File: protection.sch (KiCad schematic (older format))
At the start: 5 parts, among them Q1 DMP3098L

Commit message: Update the README, add a new rendered image of the board
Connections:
- net labels added: RP_G
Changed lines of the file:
@@
 Text Notes 2500 2700 0    50   ~ 0
 TVS should be sufficient\nto survive even some\nload dumps, at least in\nconjunction with the\npolyfuse.
-Text Notes 3750 850  0    50   ~ 0
+Text Notes 3650 950  0    50   ~ 0
 Reverse polarity protection
 Connection ~ 3350 1300
@@
 	0    1    -1   0
 $EndComp
+Text Label 4150 1650 2    50   ~ 0
+RP_G
 $EndSCHEMATC

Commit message: Make protection TVS bidirectional
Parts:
- removed D1: TPSMD16A, Diode_SMD:D_SMC, symbol Device:D_Zener
- added D1: 5.0SMDJ16CA, Diode_SMD:D_SMC, symbol Device:D_TVS
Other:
- note removed: "Fuse slightly overspecced \nregarding NMEA2000 1A\nmaximum due to strong\ntemperature derating of \npolyfuses."
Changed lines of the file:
@@
 	1    0    0    -1
-$EndComp
-$Comp
-L Device:D_Zener D?
-U 1 1 5E467AD0
-P 3000 1600
-AR Path="/5E467AD0" Ref="D?"  Part="1"
-AR Path="/5E460E30/5E467AD0" Ref="D1"  Part="1"
-F 0 "D1" V 2950 1800 50  0000 R CNN
-F 1 "TPSMD16A" V 3050 2100 50  0000 R CNN
-F 2 "Diode_SMD:D_SMC" H 3000 1600 50  0001 C CNN
-F 3 "~" H 3000 1600 50  0001 C CNN
-	1    3000 1600
-	0    -1   1    0
 $EndComp
 Wire Wire Line
@@
 Text HLabel 4900 1300 2    50   Output ~ 0
 12V_protected
-Text Notes 1500 1050 0    50   ~ 0
-Fuse slightly overspecced \nregarding NMEA2000 1A\nmaximum due to strong\ntemperature derating of \npolyfuses.
 Text Notes 2500 2700 0    50   ~ 0
 TVS should be sufficient\nto survive even some\nload dumps, at least in\nconjunction with the\npolyfuse.
@@
 Text Label 4150 1650 2    50   ~ 0
 RP_G
+$Comp
+L Device:D_TVS D1
+U 1 1 5E5A3FFE
+P 3000 1600
+F 0 "D1" V 2954 1679 50  0000 L CNN
+F 1 "5.0SMDJ16CA" V 3045 1679 50  0000 L CNN
+F 2 "Diode_SMD:D_SMC" H 3000 1600 50  0001 C CNN
+F 3 "~" H 3000 1600 50  0001 C CNN
+	1    3000 1600
+	0    1    1    0
+$EndComp
 $EndSCHEMATC

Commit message: Add LCSC part numbers to components
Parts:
- D1: LCSC (none) -> C284067
- D8: LCSC (none) -> C118608
- F1: LCSC (none) -> C135376
- Q1: LCSC (none) -> C130884
- R5: LCSC (none) -> C25803
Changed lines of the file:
@@
 F 2 "Fuse:Fuse_2920_7451Metric" V 1780 1300 50  0001 C CNN
 F 3 "~" H 1850 1300 50  0001 C CNN
+F 4 "C135376" H 1850 1300 50  0001 C CNN "LCSC"
 	1    1850 1300
 	0    1    1    0
@@
 F 2 "Package_TO_SOT_SMD:SOT-23" H 4350 1325 50  0001 L CIN
 F 3 "" H 4150 1400 50  0001 L CNN
+F 4 "C130884" H 4150 1400 50  0001 C CNN "LCSC"
 	1    4150 1400
 	0    -1   -1   0
@@
 F 2 "Diode_SMD:D_SOD-323" H 4400 1450 50  0001 C CNN
 F 3 "https://datasheet.lcsc.com/szlcsc/SK-MM3Z10_C216753.pdf" H 4400 1450 50  0001 C CNN
+F 4 "C118608" H 4400 1450 50  0001 C CNN "LCSC"
 	1    4400 1450
 	0    1    1    0
@@
 F 2 "Resistor_SMD:R_0603_1608Metric_Pad1.05x0.95mm_HandSolder" V 4080 1850 50  0001 C CNN
 F 3 "~" H 4150 1850 50  0001 C CNN
+F 4 "C25803" H 4150 1850 50  0001 C CNN "LCSC"
 	1    4150 1850
 	1    0    0    -1
@@
 F 2 "Diode_SMD:D_SMC" H 3000 1600 50  0001 C CNN
 F 3 "~" H 3000 1600 50  0001 C CNN
+F 4 "C284067" H 3000 1600 50  0001 C CNN "LCSC"
 	1    3000 1600
 	0    1    1    0

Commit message: Isolated CAN bus implementation
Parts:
- D1: value 5.0SMDJ16CA -> 5.0SMDJ20CA
- F1: value 2920L110/60MR (1.1A) -> ASMD2920-185; symbol Device:Fuse -> Device:Polyfuse; LCSC C135376 -> C135379
- R5: footprint Resistor_SMD:R_0603_1608Metric_Pad1.05x0.95mm_HandSolder -> Resistor_SMD:R_0603_1608Metric
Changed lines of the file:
@@
 $Descr A4 11693 8268
 encoding utf-8
-Sheet 7 7
+Sheet 6 7
 Title ""
 Date ""
@@
 $EndDescr
 $Comp
-L Device:Fuse F?
+L Device:Polyfuse F?
 U 1 1 5E467AC2
 P 1850 1300
@@
 AR Path="/5E460E30/5E467AC2" Ref="F1"  Part="1"
 F 0 "F1" V 1653 1300 50  0000 C CNN
-F 1 "2920L110/60MR (1.1A)" V 1744 1300 50  0000 C CNN
+F 1 "ASMD2920-185" V 1744 1300 50  0000 C CNN
 F 2 "Fuse:Fuse_2920_7451Metric" V 1780 1300 50  0001 C CNN
 F 3 "~" H 1850 1300 50  0001 C CNN
-F 4 "C135376" H 1850 1300 50  0001 C CNN "LCSC"
+F 4 "C135379" H 1850 1300 50  0001 C CNN "LCSC"
 	1    1850 1300
 	0    1    1    0
@@
 F 0 "R5" H 4220 1896 50  0000 L CNN
 F 1 "100k" H 4220 1805 50  0000 L CNN
-F 2 "Resistor_SMD:R_0603_1608Metric_Pad1.05x0.95mm_HandSolder" V 4080 1850 50  0001 C CNN
+F 2 "Resistor_SMD:R_0603_1608Metric" V 4080 1850 50  0001 C CNN
 F 3 "~" H 4150 1850 50  0001 C CNN
 F 4 "C25803" H 4150 1850 50  0001 C CNN "LCSC"
@@
 P 3000 1600
 F 0 "D1" V 2954 1679 50  0000 L CNN
-F 1 "5.0SMDJ16CA" V 3045 1679 50  0000 L CNN
+F 1 "5.0SMDJ20CA" V 3045 1679 50  0000 L CNN
 F 2 "Diode_SMD:D_SMC" H 3000 1600 50  0001 C CNN
 F 3 "~" H 3000 1600 50  0001 C CNN

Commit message: Parts updated to match JLCPCB availability
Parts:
- D8: LCSC C118608 -> C235983
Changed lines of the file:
@@
 F 2 "Diode_SMD:D_SOD-323" H 4400 1450 50  0001 C CNN
 F 3 "https://datasheet.lcsc.com/szlcsc/SK-MM3Z10_C216753.pdf" H 4400 1450 50  0001 C CNN
-F 4 "C118608" H 4400 1450 50  0001 C CNN "LCSC"
+F 4 "C235983" H 4400 1450 50  0001 C CNN "LCSC"
 	1    4400 1450
 	0    1    1    0

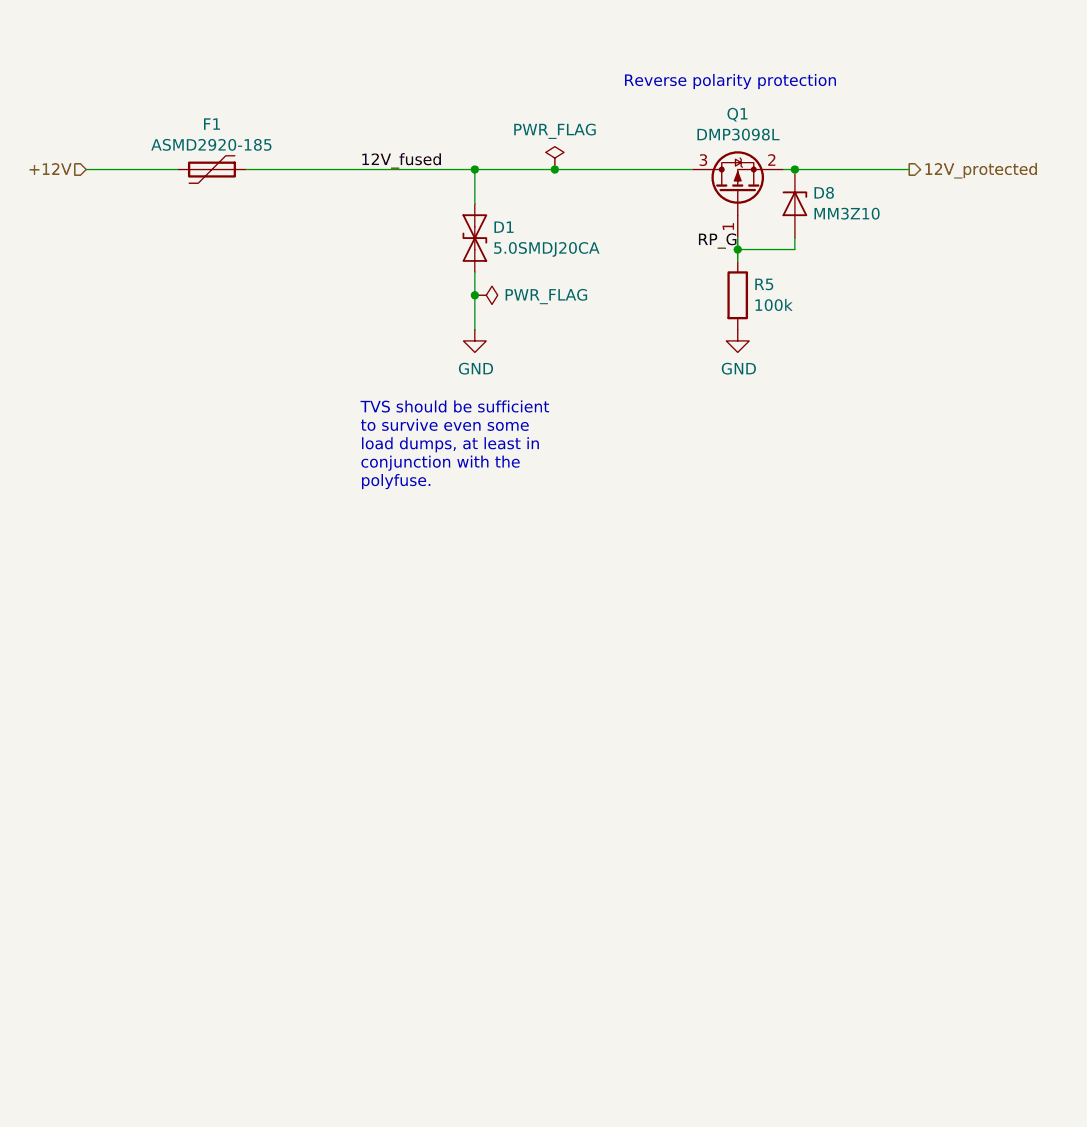
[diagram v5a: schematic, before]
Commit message: Revert back to using INA199 as a current limiter
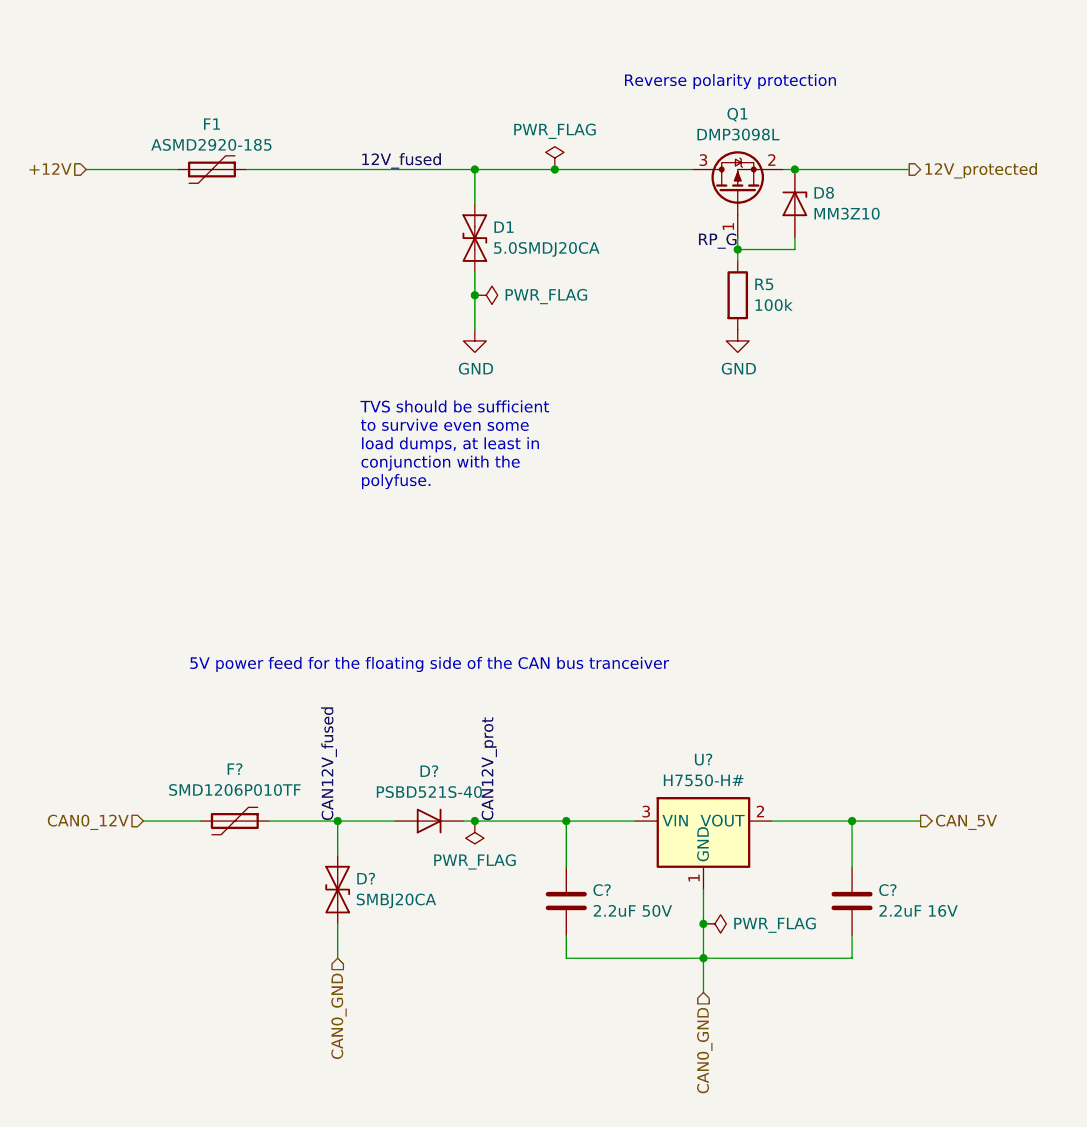
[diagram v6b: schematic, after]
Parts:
- added C?: 2.2uF 50V, Capacitor_SMD:C_1206_3216Metric, symbol Device:C
- added C?: 2.2uF 16V, Capacitor_SMD:C_0603_1608Metric, symbol Device:C
- added D?: SMBJ20CA, Diode_SMD:D_SMB, symbol Device:D_TVS
- added D?: PSBD521S-40, Diode_SMD:D_SOD-523, symbol Device:D
- added F?: SMD1206P010TF, Fuse:Fuse_1206_3216Metric, symbol Device:Polyfuse
- added U?: H7550-H#, Package_TO_SOT_SMD:SOT-23, symbol sailor-hat:HT75xx-1-SOT23
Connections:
- new net CAN0_12V: F?.2
- new net CAN0_GND: C?.2, C?.2, D?.2 (A2), U?.1 (GND)
- new net CAN12V_fused: D?.1 (A1), D?.2 (A), F?.1
- new net CAN12V_prot: C?.1, D?.1 (K), U?.3 (VIN)
- new net CAN_5V: C?.1, U?.2 (VOUT)
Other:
- note added: "5V power feed for the floating side of the CAN bus tranceiver"
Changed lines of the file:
@@
 	0    1    1    0
 $EndComp
+$Comp
+L sailor-hat:HT75xx-1-SOT23 U?
+U 1 1 5F59D8E6
+P 4000 4250
+AR Path="/5C348474/5F59D8E6" Ref="U?"  Part="1"
+AR Path="/5E460E30/5F59D8E6" Ref="U?"  Part="1"
+F 0 "U?" H 4000 4617 50  0000 C CNN
+F 1 "H7550-H#" H 4000 4526 50  0000 C CNN
+F 2 "Package_TO_SOT_SMD:SOT-23" H 4000 4575 50  0001 C CIN
+F 3 "" H 4000 4350 50  0001 C CNN
+F 4 "C277875" H 4000 4250 50  0001 C CNN "LCSC"
+	1    4000 4250
+	1    0    0    -1
+$EndComp
+$Comp
+L Device:Polyfuse F?
+U 1 1 5F59D8ED
+P 1950 4150
+AR Path="/5C348474/5F59D8ED" Ref="F?"  Part="1"
+AR Path="/5E460E30/5F59D8ED" Ref="F?"  Part="1"
+F 0 "F?" V 1725 4150 50  0000 C CNN
+F 1 "SMD1206P010TF" V 1816 4150 50  0000 C CNN
+F 2 "Fuse:Fuse_1206_3216Metric" H 2000 3950 50  0001 L CNN
+F 3 "~" H 1950 4150 50  0001 C CNN
+F 4 "C20981" H 1950 4150 50  0001 C CNN "LCSC"
+	1    1950 4150
+	0    1    1    0
+$EndComp
+$Comp
+L Device:D_TVS D?
+U 1 1 5F59D8F4
+P 2400 4450
+AR Path="/5C348474/5F59D8F4" Ref="D?"  Part="1"
+AR Path="/5E460E30/5F59D8F4" Ref="D?"  Part="1"
+F 0 "D?" V 2354 4529 50  0000 L CNN
+F 1 "SMBJ20CA" V 2445 4529 50  0000 L CNN
+F 2 "Diode_SMD:D_SMB" H 2400 4450 50  0001 C CNN
+F 3 "~" H 2400 4450 50  0001 C CNN
+F 4 "C113992" H 2400 4450 50  0001 C CNN "LCSC"
+	1    2400 4450
+	0    1    1    0
+$EndComp
+$Comp
+L Device:D D?
+U 1 1 5F59D8FB
+P 2800 4150
+AR Path="/5C348474/5F59D8FB" Ref="D?"  Part="1"
+AR Path="/5E460E30/5F59D8FB" Ref="D?"  Part="1"
+F 0 "D?" H 2800 3934 50  0000 C CNN
+F 1 "PSBD521S-40" H 2800 4025 50  0000 C CNN
+F 2 "Diode_SMD:D_SOD-523" H 2800 4150 50  0001 C CNN
+F 3 "~" H 2800 4150 50  0001 C CNN
+F 4 "C168633" H 2800 4150 50  0001 C CNN "LCSC"
+	1    2800 4150
+	-1   0    0    1
+$EndComp
+Wire Wire Line
+	2100 4150 2400 4150
+Wire Wire Line
+	2950 4150 3000 4150
+Wire Wire Line
+	4000 4900 4000 4750
+Wire Wire Line
+	2400 4300 2400 4150
+Connection ~ 2400 4150
+Wire Wire Line
+	2400 4150 2650 4150
+Wire Wire Line
+	2400 4600 2400 4750
+Text HLabel 1550 4150 0    50   Input ~ 0
+CAN0_12V
+Text HLabel 2400 4750 3    50   Input ~ 0
+CAN0_GND
+Text HLabel 4000 4900 3    50   Input ~ 0
+CAN0_GND
+Text Notes 1750 3500 0    50   ~ 0
+5V power feed for the floating side of the CAN bus tranceiver
+$Comp
+L power:PWR_FLAG #FLG?
+U 1 1 5F59D90D
+P 3000 4150
+AR Path="/5C348474/5F59D90D" Ref="#FLG?"  Part="1"
+AR Path="/5E460E30/5F59D90D" Ref="#FLG0107"  Part="1"
+F 0 "#FLG0107" H 3000 4225 50  0001 C CNN
+F 1 "PWR_FLAG" H 3000 4323 50  0000 C CNN
+F 2 "" H 3000 4150 50  0001 C CNN
+F 3 "~" H 3000 4150 50  0001 C CNN
+	1    3000 4150
+	-1   0    0    1
+$EndComp
+Connection ~ 3000 4150
+Wire Wire Line
+	3000 4150 3400 4150
+$Comp
+L power:PWR_FLAG #FLG?
+U 1 1 5F59D915
+P 4000 4600
+AR Path="/5C348474/5F59D915" Ref="#FLG?"  Part="1"
+AR Path="/5E460E30/5F59D915" Ref="#FLG0108"  Part="1"
+F 0 "#FLG0108" H 4000 4675 50  0001 C CNN
+F 1 "PWR_FLAG" V 4000 4728 50  0000 L CNN
+F 2 "" H 4000 4600 50  0001 C CNN
+F 3 "~" H 4000 4600 50  0001 C CNN
+	1    4000 4600
+	0    1    1    0
+$EndComp
+Connection ~ 4000 4600
+Wire Wire Line
+	4000 4600 4000 4450
+Wire Wire Line
+	1550 4150 1800 4150
+Text Label 2400 4150 1    50   ~ 0
+CAN12V_fused
+Text Label 3100 4150 1    50   ~ 0
+CAN12V_prot
+$Comp
+L Device:C C?
+U 1 1 5F59D921
+P 3400 4500
+AR Path="/5CA65CC5/5F59D921" Ref="C?"  Part="1"
+AR Path="/5C348474/5F59D921" Ref="C?"  Part="1"
+AR Path="/5E460E30/5F59D921" Ref="C?"  Part="1"
+F 0 "C?" H 3515 4546 50  0000 L CNN
+F 1 "2.2uF 50V" H 3515 4455 50  0000 L CNN
+F 2 "Capacitor_SMD:C_1206_3216Metric" H 3438 4350 50  0001 C CNN
+F 3 "~" H 3400 4500 50  0001 C CNN
+F 4 "C50254" H 3400 4500 50  0001 C CNN "LCSC"
+	1    3400 4500
+	1    0    0    -1
+$EndComp
+$Comp
+L Device:C C?
+U 1 1 5F59D928
+P 4650 4500
+AR Path="/5CA65CC5/5F59D928" Ref="C?"  Part="1"
+AR Path="/5C348474/5F59D928" Ref="C?"  Part="1"
+AR Path="/5E460E30/5F59D928" Ref="C?"  Part="1"
+F 0 "C?" H 4765 4546 50  0000 L CNN
+F 1 "2.2uF 16V" H 4765 4455 50  0000 L CNN
+F 2 "Capacitor_SMD:C_0603_1608Metric" H 4688 4350 50  0001 C CNN
+F 3 "~" H 4650 4500 50  0001 C CNN
+F 4 "C23630" H 4650 4500 50  0001 C CNN "LCSC"
+	1    4650 4500
+	1    0    0    -1
+$EndComp
+Wire Wire Line
+	3400 4350 3400 4150
+Connection ~ 3400 4150
+Wire Wire Line
+	3400 4150 3700 4150
+Wire Wire Line
+	4650 4350 4650 4150
+Wire Wire Line
+	4650 4150 4300 4150
+Wire Wire Line
+	4950 4150 4650 4150
+Connection ~ 4650 4150
+Wire Wire Line
+	3400 4650 3400 4750
+Wire Wire Line
+	3400 4750 4000 4750
+Connection ~ 4000 4750
+Wire Wire Line
+	4000 4750 4000 4600
+Wire Wire Line
+	4000 4750 4650 4750
+Wire Wire Line
+	4650 4750 4650 4650
+Text HLabel 4950 4150 2    50   Output ~ 0
+CAN_5V
 $EndSCHEMATC

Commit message: Make voltage protection circuitry 24V compliant
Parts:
- D1: value 5.0SMDJ20CA -> 5.0SMDJ36CA; LCSC C284067 -> C284112
- D10: renamed from D?; value SMBJ20CA -> SMBJ36CA; LCSC C113992 -> C114002
- D13: renamed from D?; value PSBD521S-40 -> SS210; footprint Diode_SMD:D_SOD-523 -> Diode_SMD:D_SMA; symbol Device:D -> Device:D_Schottky
- D8: value MM3Z10 -> MM3Z8V2; LCSC C235983 -> C118606
- Q1: value DMP3098L -> WST03P06; LCSC C130884 -> C105166
- gave numbers to parts that had none: 4
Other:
- note added: "5V power feed for the bus side of the CAN bus tranceiver"
- note removed: "5V power feed for the floating side of the CAN bus tranceiver"
- note removed: "TVS should be sufficient\nto survive even some\nload dumps, at least in\nconjunction with the\npolyfuse."
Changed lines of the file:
@@
 AR Path="/5E460E30/5E467ADC" Ref="Q1"  Part="1"
 F 0 "Q1" V 4492 1400 50  0000 C CNN
-F 1 "DMP3098L" V 4401 1400 50  0000 C CNN
+F 1 "WST03P06" V 4401 1400 50  0000 C CNN
 F 2 "Package_TO_SOT_SMD:SOT-23" H 4350 1325 50  0001 L CIN
 F 3 "" H 4150 1400 50  0001 L CNN
-F 4 "C130884" H 4150 1400 50  0001 C CNN "LCSC"
+F 4 "C105166" H 4150 1400 50  0001 C CNN "LCSC"
 	1    4150 1400
 	0    -1   -1   0
@@
 AR Path="/5E460E30/5E467AE2" Ref="D8"  Part="1"
 F 0 "D8" V 4354 1529 50  0000 L CNN
-F 1 "MM3Z10" V 4445 1529 50  0000 L CNN
+F 1 "MM3Z8V2" V 4445 1529 50  0000 L CNN
 F 2 "Diode_SMD:D_SOD-323" H 4400 1450 50  0001 C CNN
-F 3 "https://datasheet.lcsc.com/szlcsc/SK-MM3Z10_C216753.pdf" H 4400 1450 50  0001 C CNN
-F 4 "C235983" H 4400 1450 50  0001 C CNN "LCSC"
+F 3 "" H 4400 1450 50  0001 C CNN
+F 4 "C118606" H 4400 1450 50  0001 C CNN "LCSC"
 	1    4400 1450
 	0    1    1    0
@@
 Text HLabel 4900 1300 2    50   Output ~ 0
 12V_protected
-Text Notes 2500 2700 0    50   ~ 0
-TVS should be sufficient\nto survive even some\nload dumps, at least in\nconjunction with the\npolyfuse.
 Text Notes 3650 950  0    50   ~ 0
 Reverse polarity protection
@@
 P 3000 1600
 F 0 "D1" V 2954 1679 50  0000 L CNN
-F 1 "5.0SMDJ20CA" V 3045 1679 50  0000 L CNN
+F 1 "5.0SMDJ36CA" V 3045 1679 50  0000 L CNN
 F 2 "Diode_SMD:D_SMC" H 3000 1600 50  0001 C CNN
 F 3 "~" H 3000 1600 50  0001 C CNN
-F 4 "C284067" H 3000 1600 50  0001 C CNN "LCSC"
+F 4 "C284112" H 3000 1600 50  0001 C CNN "LCSC"
 	1    3000 1600
 	0    1    1    0
@@
 P 4000 4250
 AR Path="/5C348474/5F59D8E6" Ref="U?"  Part="1"
-AR Path="/5E460E30/5F59D8E6" Ref="U?"  Part="1"
-F 0 "U?" H 4000 4617 50  0000 C CNN
+AR Path="/5E460E30/5F59D8E6" Ref="U7"  Part="1"
+F 0 "U7" H 4000 4617 50  0000 C CNN
 F 1 "H7550-H#" H 4000 4526 50  0000 C CNN
 F 2 "Package_TO_SOT_SMD:SOT-23" H 4000 4575 50  0001 C CIN
@@
 P 1950 4150
 AR Path="/5C348474/5F59D8ED" Ref="F?"  Part="1"
-AR Path="/5E460E30/5F59D8ED" Ref="F?"  Part="1"
-F 0 "F?" V 1725 4150 50  0000 C CNN
+AR Path="/5E460E30/5F59D8ED" Ref="F2"  Part="1"
+F 0 "F2" V 1725 4150 50  0000 C CNN
 F 1 "SMD1206P010TF" V 1816 4150 50  0000 C CNN
 F 2 "Fuse:Fuse_1206_3216Metric" H 2000 3950 50  0001 L CNN
@@
 P 2400 4450
 AR Path="/5C348474/5F59D8F4" Ref="D?"  Part="1"
-AR Path="/5E460E30/5F59D8F4" Ref="D?"  Part="1"
-F 0 "D?" V 2354 4529 50  0000 L CNN
-F 1 "SMBJ20CA" V 2445 4529 50  0000 L CNN
+AR Path="/5E460E30/5F59D8F4" Ref="D10"  Part="1"
+F 0 "D10" V 2354 4529 50  0000 L CNN
+F 1 "SMBJ36CA" V 2445 4529 50  0000 L CNN
 F 2 "Diode_SMD:D_SMB" H 2400 4450 50  0001 C CNN
 F 3 "~" H 2400 4450 50  0001 C CNN
-F 4 "C113992" H 2400 4450 50  0001 C CNN "LCSC"
+F 4 "C114002" H 2400 4450 50  0001 C CNN "LCSC"
 	1    2400 4450
 	0    1    1    0
 $EndComp
 $Comp
-L Device:D D?
+L Device:D_Schottky D?
 U 1 1 5F59D8FB
 P 2800 4150
 AR Path="/5C348474/5F59D8FB" Ref="D?"  Part="1"
-AR Path="/5E460E30/5F59D8FB" Ref="D?"  Part="1"
-F 0 "D?" H 2800 3934 50  0000 C CNN
-F 1 "PSBD521S-40" H 2800 4025 50  0000 C CNN
-F 2 "Diode_SMD:D_SOD-523" H 2800 4150 50  0001 C CNN
+AR Path="/5E460E30/5F59D8FB" Ref="D13"  Part="1"
+F 0 "D13" H 2800 3934 50  0000 C CNN
+F 1 "SS210" H 2800 4025 50  0000 C CNN
+F 2 "Diode_SMD:D_SMA" H 2800 4150 50  0001 C CNN
 F 3 "~" H 2800 4150 50  0001 C CNN
 F 4 "C168633" H 2800 4150 50  0001 C CNN "LCSC"
@@
 	2100 4150 2400 4150
 Wire Wire Line
-	2950 4150 3000 4150
+	2950 4150 3150 4150
 Wire Wire Line
 	4000 4900 4000 4750
@@
 CAN0_GND
 Text Notes 1750 3500 0    50   ~ 0
-5V power feed for the floating side of the CAN bus tranceiver
+5V power feed for the bus side of the CAN bus tranceiver
 $Comp
 L power:PWR_FLAG #FLG?
 U 1 1 5F59D90D
-P 3000 4150
+P 3150 4150
 AR Path="/5C348474/5F59D90D" Ref="#FLG?"  Part="1"
 AR Path="/5E460E30/5F59D90D" Ref="#FLG0107"  Part="1"
-F 0 "#FLG0107" H 3000 4225 50  0001 C CNN
-F 1 "PWR_FLAG" H 3000 4323 50  0000 C CNN
-F 2 "" H 3000 4150 50  0001 C CNN
-F 3 "~" H 3000 4150 50  0001 C CNN
-	1    3000 4150
+F 0 "#FLG0107" H 3150 4225 50  0001 C CNN
+F 1 "PWR_FLAG" H 3150 4323 50  0000 C CNN
+F 2 "" H 3150 4150 50  0001 C CNN
+F 3 "~" H 3150 4150 50  0001 C CNN
+	1    3150 4150
 	-1   0    0    1
 $EndComp
-Connection ~ 3000 4150
-Wire Wire Line
-	3000 4150 3400 4150
+Connection ~ 3150 4150
+Wire Wire Line
+	3150 4150 3400 4150
 $Comp
 L power:PWR_FLAG #FLG?
@@
 Text Label 2400 4150 1    50   ~ 0
 CAN12V_fused
-Text Label 3100 4150 1    50   ~ 0
+Text Label 3300 4150 1    50   ~ 0
 CAN12V_prot
 $Comp
@@
 AR Path="/5CA65CC5/5F59D921" Ref="C?"  Part="1"
 AR Path="/5C348474/5F59D921" Ref="C?"  Part="1"
-AR Path="/5E460E30/5F59D921" Ref="C?"  Part="1"
-F 0 "C?" H 3515 4546 50  0000 L CNN
+AR Path="/5E460E30/5F59D921" Ref="C11"  Part="1"
+F 0 "C11" H 3515 4546 50  0000 L CNN
 F 1 "2.2uF 50V" H 3515 4455 50  0000 L CNN
 F 2 "Capacitor_SMD:C_1206_3216Metric" H 3438 4350 50  0001 C CNN
@@
 AR Path="/5CA65CC5/5F59D928" Ref="C?"  Part="1"
 AR Path="/5C348474/5F59D928" Ref="C?"  Part="1"
-AR Path="/5E460E30/5F59D928" Ref="C?"  Part="1"
-F 0 "C?" H 4765 4546 50  0000 L CNN
+AR Path="/5E460E30/5F59D928" Ref="C15"  Part="1"
+F 0 "C15" H 4765 4546 50  0000 L CNN
 F 1 "2.2uF 16V" H 4765 4455 50  0000 L CNN
 F 2 "Capacitor_SMD:C_0603_1608Metric" H 4688 4350 50  0001 C CNN

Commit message: Swap CAN power rectifier diode into a smaller one
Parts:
- D13: value SS210 -> SM4007PL; footprint Diode_SMD:D_SMA -> Diode_SMD:D_SOD-123F; symbol Device:D_Schottky -> Device:D; LCSC C168633 -> C64898
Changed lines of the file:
@@
 $EndComp
 $Comp
-L Device:D_Schottky D?
+L Device:D D?
 U 1 1 5F59D8FB
 P 2800 4150
@@
 AR Path="/5E460E30/5F59D8FB" Ref="D13"  Part="1"
 F 0 "D13" H 2800 3934 50  0000 C CNN
-F 1 "SS210" H 2800 4025 50  0000 C CNN
-F 2 "Diode_SMD:D_SMA" H 2800 4150 50  0001 C CNN
+F 1 "SM4007PL" H 2800 4025 50  0000 C CNN
+F 2 "Diode_SMD:D_SOD-123F" H 2800 4150 50  0001 C CNN
 F 3 "~" H 2800 4150 50  0001 C CNN
-F 4 "C168633" H 2800 4150 50  0001 C CNN "LCSC"
+F 4 "C64898" H 2800 4150 50  0001 C CNN "LCSC"
 	1    2800 4150
 	-1   0    0    1
